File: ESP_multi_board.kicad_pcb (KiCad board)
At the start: 2 copper layers, 22 parts, among them P101 CONN_01X02, P102 CONN_01X06, P103 CONN_01X02, P104 CONN_01X06, P105 CONN_01X12, P106 CONN_01X03, P108 CONN_I2C_MPU6050, P110 CONN_PINES_DIG, U1 LD1117S33TR, U101 L293DD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

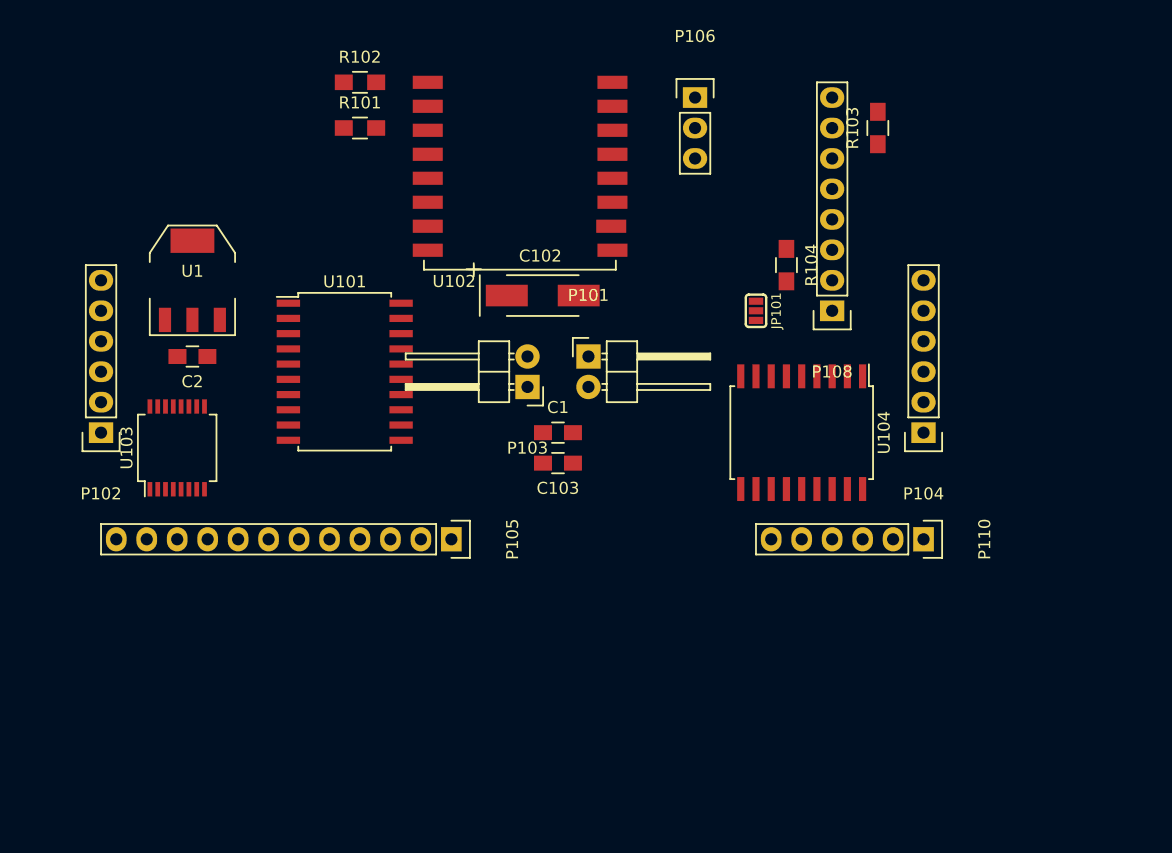
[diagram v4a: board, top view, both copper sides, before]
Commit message: cambio de posiciones en la placa
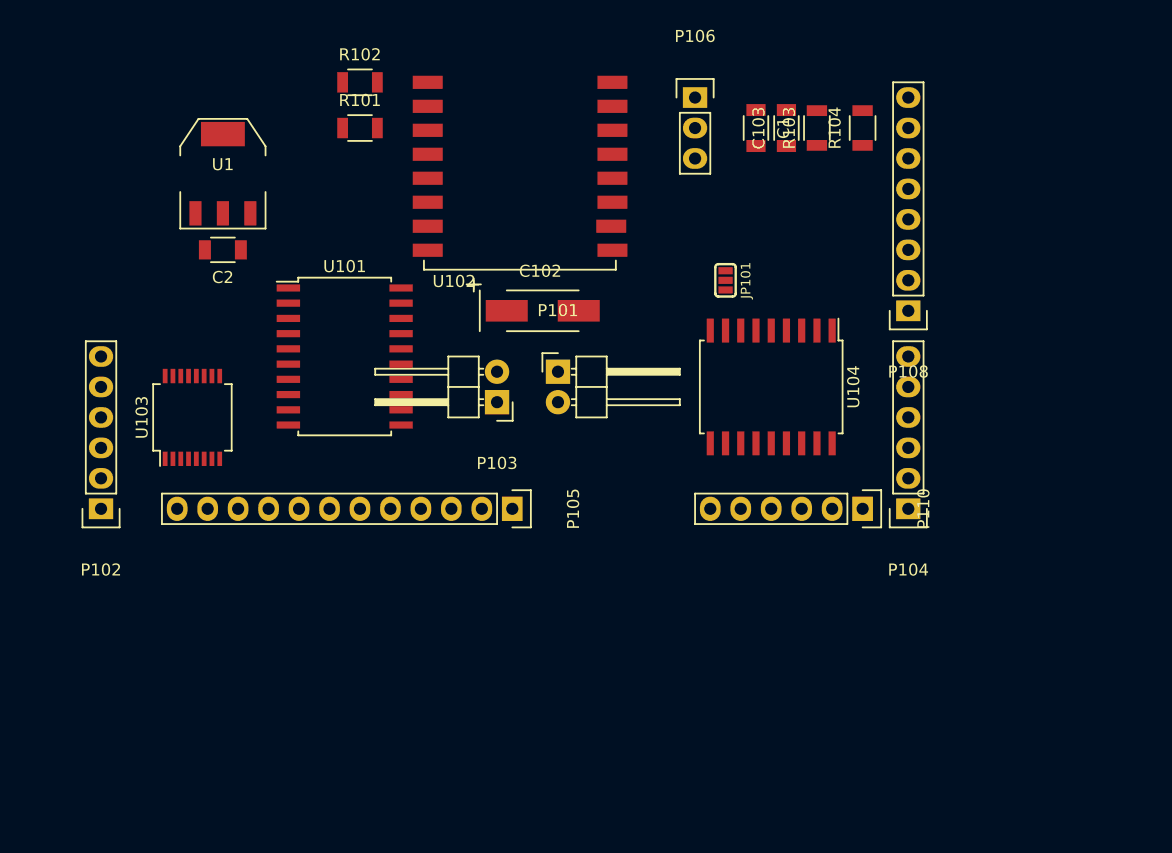
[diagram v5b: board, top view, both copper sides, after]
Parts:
- C1, C103, C2: footprint Capacitors_SMD:C_0805_HandSoldering -> Capacitors_SMD:C_1206
- R101, R102, R103, R104: footprint Resistors_SMD:R_0805_HandSoldering -> Resistors_SMD:R_1206
- moved C103 33.8 mm to (174.0, 62.2), turned to 90 degrees
- moved C1 30.3 mm to (171.4, 62.2), turned to 270 degrees
- moved R104 13.1 mm to (180.3, 62.2), turned to 90 degrees
- moved C2 9.25 mm to (127.0, 72.4)
- moved U1 9.25 mm to (127.0, 66.0)
- moved P104 6.48 mm to (184.2, 94.0)
- moved P102 6.35 mm to (116.8, 94.0)
- moved P108 6.35 mm to (184.2, 77.5)
- moved P105 5.68 mm to (151.1, 94.0)
- moved P110 5.68 mm to (180.3, 94.0)
- moved R103 5.08 mm to (176.5, 62.2)
- moved U104 4.58 mm to (172.7, 83.8)
- moved JP101 3.59 mm to (168.9, 74.9)
- moved U103 2.84 mm to (124.5, 86.4)
- moved P103 2.84 mm to (149.9, 85.1)
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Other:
- net class Default: clearance 0.2 -> 0.3; trace_width 0.25 -> 0.3
- rule trace_clearance: 0.2 -> 0.3
- rule trace_min: 0.2 -> 0.3
- rule via_min_size: 0.4 -> 0.3

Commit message: versión quasifinal
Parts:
- added R103: 10k, Resistors_SMD:R_1206, F.Cu at (163.8, 71.1)
- added R104: 10k, Resistors_SMD:R_1206, F.Cu at (166.4, 71.1)
- added SW101: SW_PUSH_SMALL, Buttons_Switches_SMD:SW_SPST_EVPBF, F.Cu at (118.1, 62.2)
- added SW102: SW_PUSH_SMALL, Buttons_Switches_SMD:SW_SPST_EVPBF, F.Cu at (175.3, 69.8)
- renumbered C102 to C101, C103 to C102, P108 to P107, P110 to P108, R103 to R105, R104 to R106
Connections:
- U102 pad 10: ENC2_A -> GPIO0
- U102 pad 11: ENC1_A -> EN1
- U102 pad 12: GPIO0 -> SCL
- U102 pad 14: SCL -> EN2
- U102 pad 4: EN1 -> ENC1_A
- U102 pad 5: EN2 -> ENC2_A

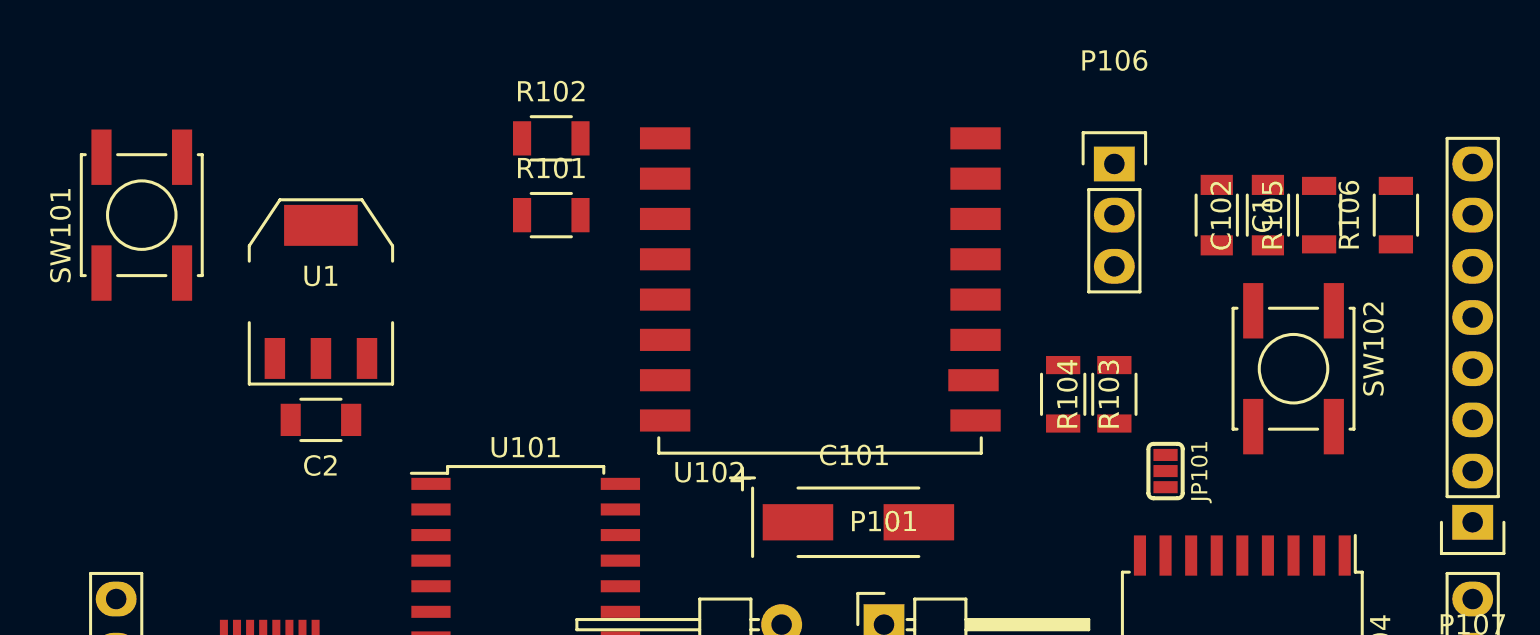
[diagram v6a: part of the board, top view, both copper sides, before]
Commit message: vesion simplificada, sin jumper y sinconectar los pines de int
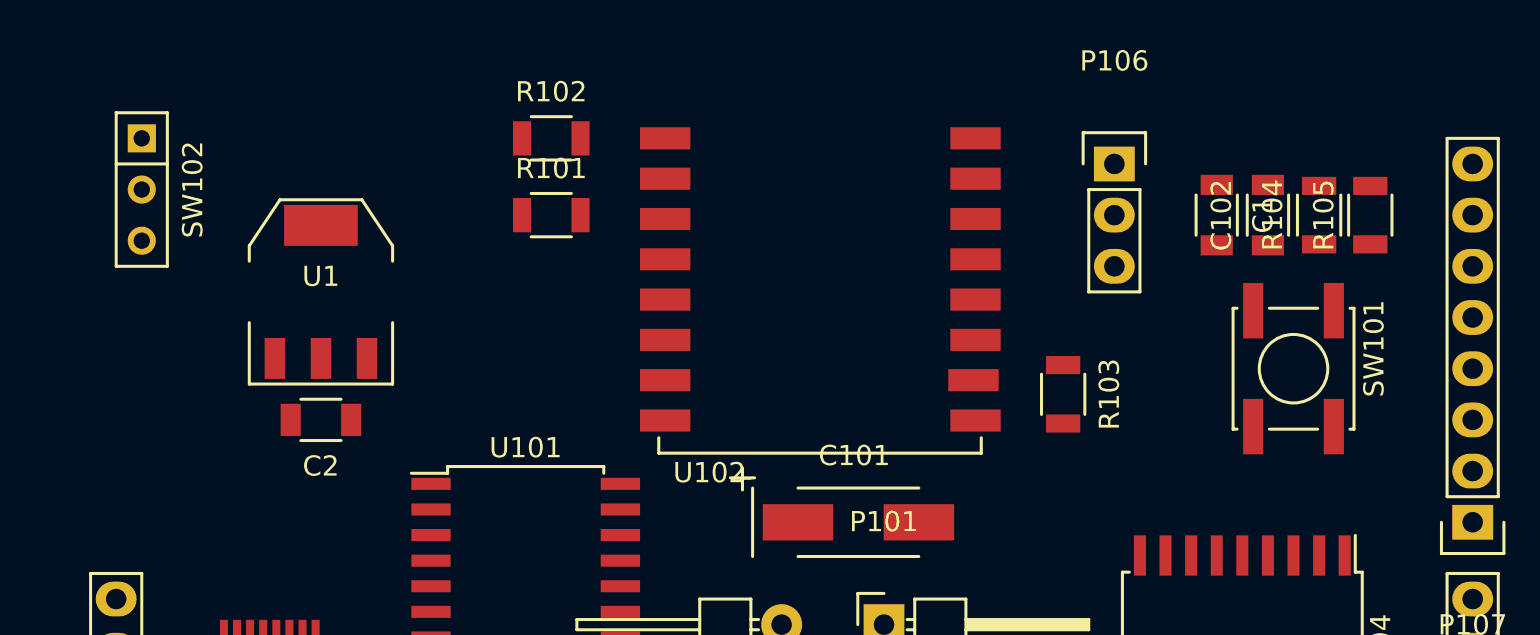
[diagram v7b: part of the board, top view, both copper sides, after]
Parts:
- removed JP101: JUMPER3, keyboard_parts:SOLDER_JUMPER_3
- removed the R104 at (166.4, 71.1)
- removed the SW101 at (118.1, 62.2)
- added SW102: SWITCH_INV, Buttons_Switches_ThroughHole:SW_Micro_SPST, F.Cu at (118.1, 61.0)
- moved R105 1.27 mm to (179.1, 62.2)
- renumbered R105 to R104, R106 to R105, SW102 to SW101
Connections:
- net GPIO0 renamed Net-(R103-Pad1)
- C1 pad 1: VDD -> /reg5to3_3V/3_3V
- P107 pad 1: Net-(JP101-Pad1) -> (no net)
- U1 pad 2: VDD -> /reg5to3_3V/3_3V
- U104 pad 8: Net-(JP101-Pad3) -> (no net)

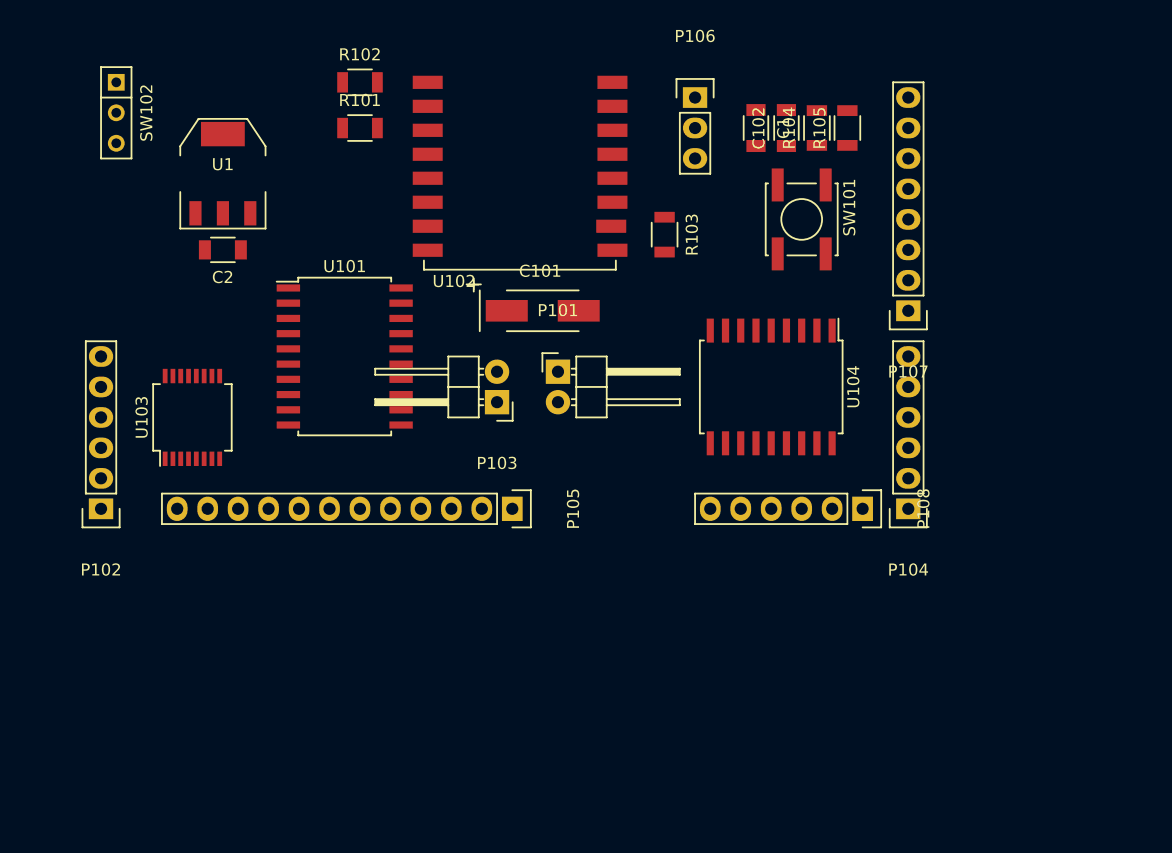
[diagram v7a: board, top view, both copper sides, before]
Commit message: cambio de posición ADC y L293DD
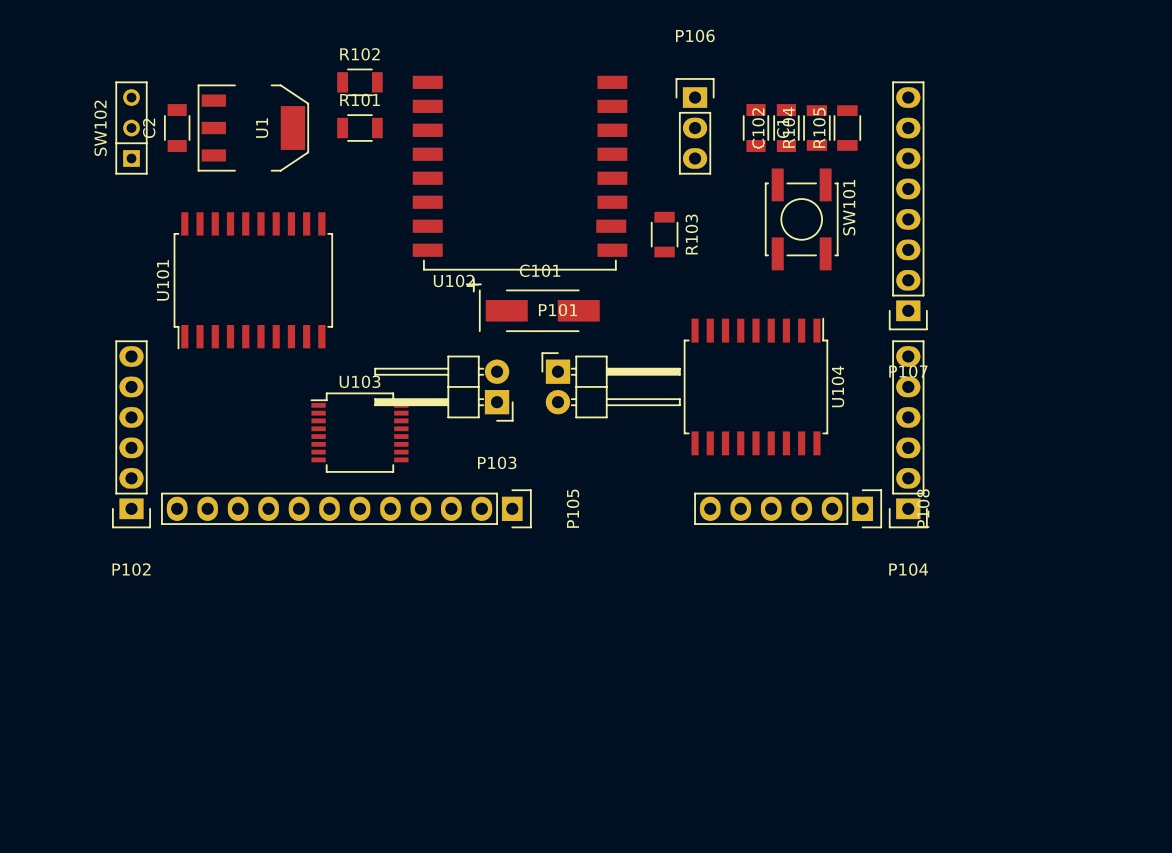
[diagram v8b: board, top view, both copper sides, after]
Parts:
- moved U103 14.0 mm to (138.4, 87.6), turned to 0 degrees
- moved C2 10.9 mm to (123.2, 62.2), turned to 90 degrees
- moved U101 9.92 mm to (129.5, 74.9), turned to 90 degrees
- moved U1 4.58 mm to (129.5, 62.2), turned to 270 degrees
- moved P102 2.54 mm to (119.4, 94.0)
- moved SW102 1.80 mm to (119.4, 62.2), turned to 90 degrees
- moved U104 1.27 mm to (171.4, 83.8)
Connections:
- U103 pad 10: Net-(P105-Pad2) -> Net-(P105-Pad3)
- U103 pad 11: Net-(P105-Pad3) -> Net-(P105-Pad2)
- U103 pad 12: Net-(P105-Pad4) -> Net-(P105-Pad1)
- U103 pad 6: Net-(P105-Pad7) -> Net-(P105-Pad5)
- U103 pad 8: Net-(P105-Pad5) -> Net-(P105-Pad7)
- U103 pad 9: Net-(P105-Pad1) -> Net-(P105-Pad4)
